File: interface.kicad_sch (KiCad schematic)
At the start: 6 parts, among them J2 M20-7810245, J3 M20-7812045, J4 M20-7812045

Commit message: Board is fully routed
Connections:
- net 12V: no longer names the net of J4.1 (+12V)
- net 12V: no longer J3.1 (+12V)
- no-connect marks 58 -> 60
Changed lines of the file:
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@@
   (junction (at 134.62 72.39) (diameter 0) (color 0 0 0 0)
-  )
-  (junction (at 73.66 46.99) (diameter 0) (color 0 0 0 0)
   )
   (junction (at 134.62 85.09) (diameter 0) (color 0 0 0 0)
@@
   (no_connect (at 77.47 92.71))
   (no_connect (at 102.87 92.71))
+  (no_connect (at 77.47 46.99))
   (no_connect (at 137.16 67.31))
   (no_connect (at 137.16 95.25))
@@
   (no_connect (at 102.87 77.47))
   (no_connect (at 137.16 62.23))
+  (no_connect (at 137.16 46.99))
   (no_connect (at 137.16 80.01))
   (no_connect (at 77.47 49.53))
@@
     (stroke (width 0) (type default))
   )
-  (wire (pts (xy 64.77 46.99) (xy 73.66 46.99))
-    (stroke (width 0) (type default))
-  )
   (wire (pts (xy 256.54 44.45) (xy 254 44.45))
     (stroke (width 0) (type default))
@@
     (stroke (width 0) (type default))
   )
-  (wire (pts (xy 133.35 43.18) (xy 133.35 46.99))
-    (stroke (width 0) (type default))
-  )
   (wire (pts (xy 238.76 91.44) (xy 238.76 93.98))
     (stroke (width 0) (type default))
@@
     (stroke (width 0) (type default))
   )
-  (wire (pts (xy 73.66 46.99) (xy 77.47 46.99))
-    (stroke (width 0) (type default))
-  )
   (wire (pts (xy 63.5 69.85) (xy 77.47 69.85))
     (stroke (width 0) (type default))
@@
     (stroke (width 0) (type default))
   )
-  (wire (pts (xy 73.66 43.18) (xy 73.66 46.99))
-    (stroke (width 0) (type default))
-  )
   (wire (pts (xy 105.41 85.09) (xy 105.41 104.14))
     (stroke (width 0) (type default))
@@
   )
   (wire (pts (xy 77.47 59.69) (xy 74.93 59.69))
-    (stroke (width 0) (type default))
-  )
-  (wire (pts (xy 133.35 46.99) (xy 137.16 46.99))
-    (stroke (width 0) (type default))
-  )
-  (wire (pts (xy 64.77 43.18) (xy 64.77 46.99))
     (stroke (width 0) (type default))
   )
@@
         (path "/b3f993c3-1966-49ed-ad69-98ff713d15d5/022f9d20-4e59-4748-8eac-9224ddae6c41"
           (reference "#PWR06") (unit 1)
-        )
-      )
-    )
-  )
-  (symbol (lib_id "sesa_power:12V") (at 133.35 43.18 0) (unit 1)
-    (in_bom yes) (on_board yes) (dnp no)
-    (property "Reference" "#PWR01" (at 133.35 40.64 0)
-      (effects (font (size 1.016 1.016)) hide)
-    )
-    (property "Value" "12V" (at 133.35 40.513 0)
-      (effects (font (size 1.27 1.27)))
-    )
-    (property "Footprint" "" (at 133.35 43.18 0)
-      (effects (font (size 1.27 1.27)))
-    )
-    (property "Datasheet" "" (at 133.35 43.18 0)
-      (effects (font (size 1.27 1.27)))
-    )
-    (pin "1")
-    (instances
-      (project "DMM_Module"
-        (path "/b3f993c3-1966-49ed-ad69-98ff713d15d5/022f9d20-4e59-4748-8eac-9224ddae6c41"
-          (reference "#PWR01") (unit 1)
         )
       )
@@
         )
       )
-    )
-  )
-  (symbol (lib_id "sesa_power:12V") (at 73.66 43.18 0) (unit 1)
-    (in_bom yes) (on_board yes) (dnp no)
-    (property "Reference" "#PWR04" (at 73.66 40.64 0)
-      (effects (font (size 1.016 1.016)) hide)
-    )
-    (property "Value" "12V" (at 73.66 40.513 0)
-      (effects (font (size 1.27 1.27)))
-    )
-    (property "Footprint" "" (at 73.66 43.18 0)
-      (effects (font (size 1.27 1.27)))
-    )
-    (property "Datasheet" "" (at 73.66 43.18 0)
-      (effects (font (size 1.27 1.27)))
-    )
-    (pin "1")
-    (instances
-      (project "DMM_Module"
-        (path "/b3f993c3-1966-49ed-ad69-98ff713d15d5/022f9d20-4e59-4748-8eac-9224ddae6c41"
-          (reference "#PWR04") (unit 1)
-        )
-      )
-    )
-  )
-  (symbol (lib_id "sesa_power:PWR_PORT") (at 64.77 43.18 0) (unit 1)
-    (in_bom yes) (on_board yes) (dnp no)
-    (property "Reference" "#PWR09" (at 64.77 40.64 0)
-      (effects (font (size 1.016 1.016)) hide)
-    )
-    (property "Value" "PWR_PORT" (at 64.77 40.513 0)
-      (effects (font (size 1.27 1.27)))
-    )
-    (property "Footprint" "" (at 64.77 43.18 0)
-      (effects (font (size 1.27 1.27)))
-    )
-    (property "Datasheet" "" (at 64.77 43.18 0)
-      (effects (font (size 1.27 1.27)))
-    )
-    (pin "1")
-    (instances
-      (project "DMM_Module"
-        (path "/b3f993c3-1966-49ed-ad69-98ff713d15d5/0095a40f-579d-4b0e-95e8-5fdd46ee20e8"
-          (reference "#PWR09") (unit 1)
-        )
-        (path "/b3f993c3-1966-49ed-ad69-98ff713d15d5/022f9d20-4e59-4748-8eac-9224ddae6c41"
-          (reference "#PWR060") (unit 1)
-        )
-      )

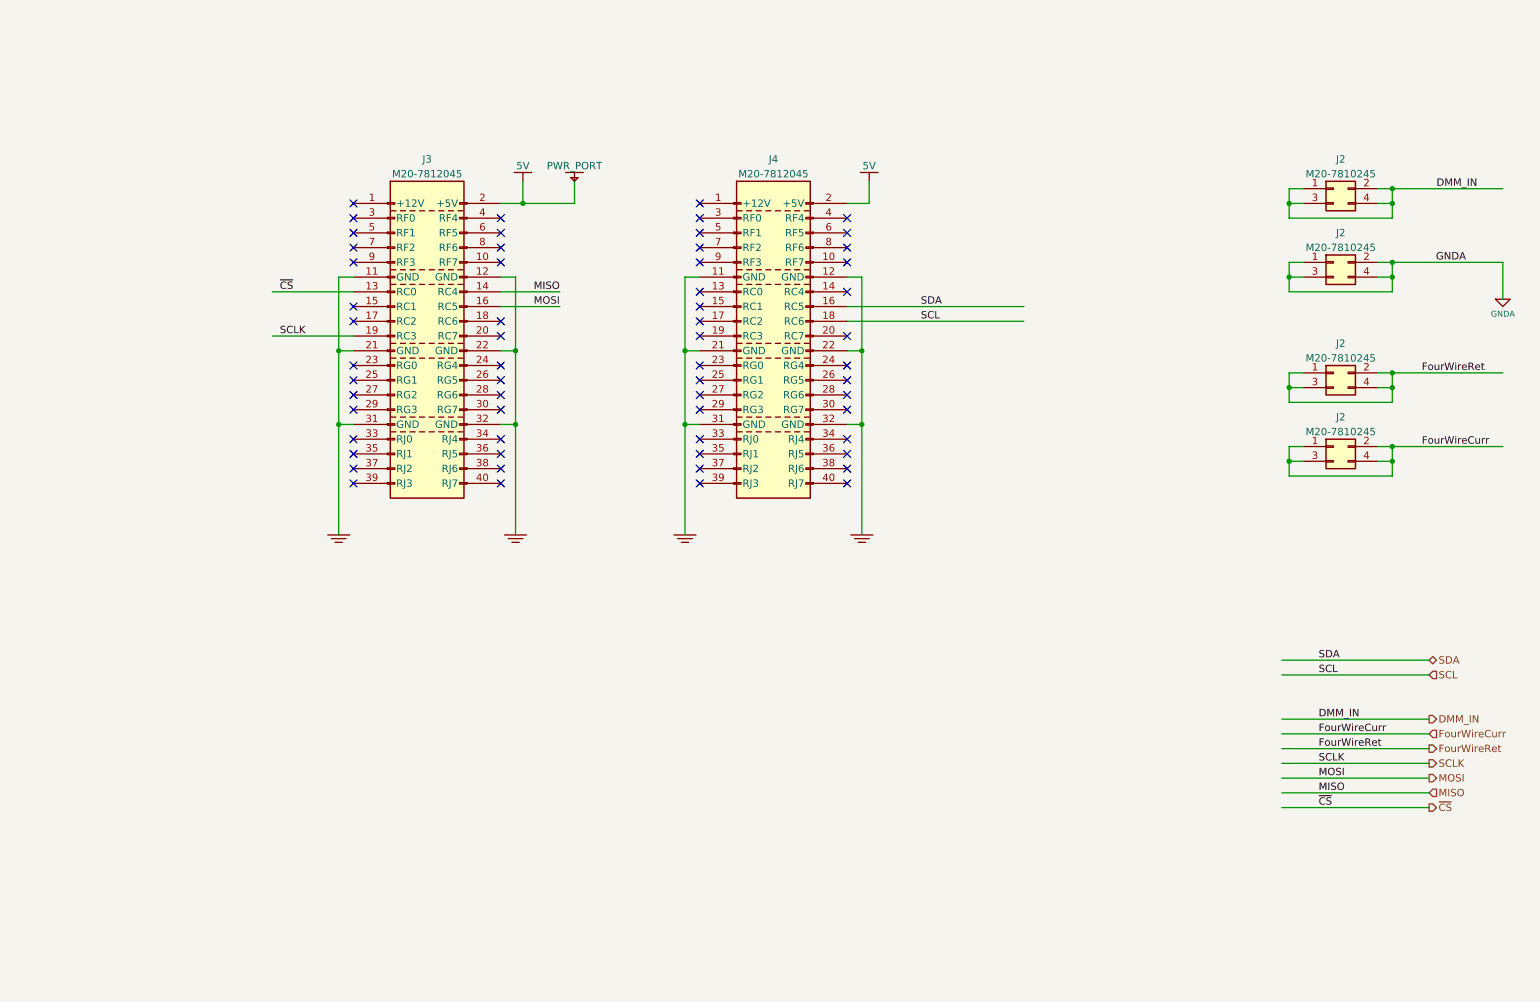
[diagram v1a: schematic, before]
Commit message: Added galvanic isolation
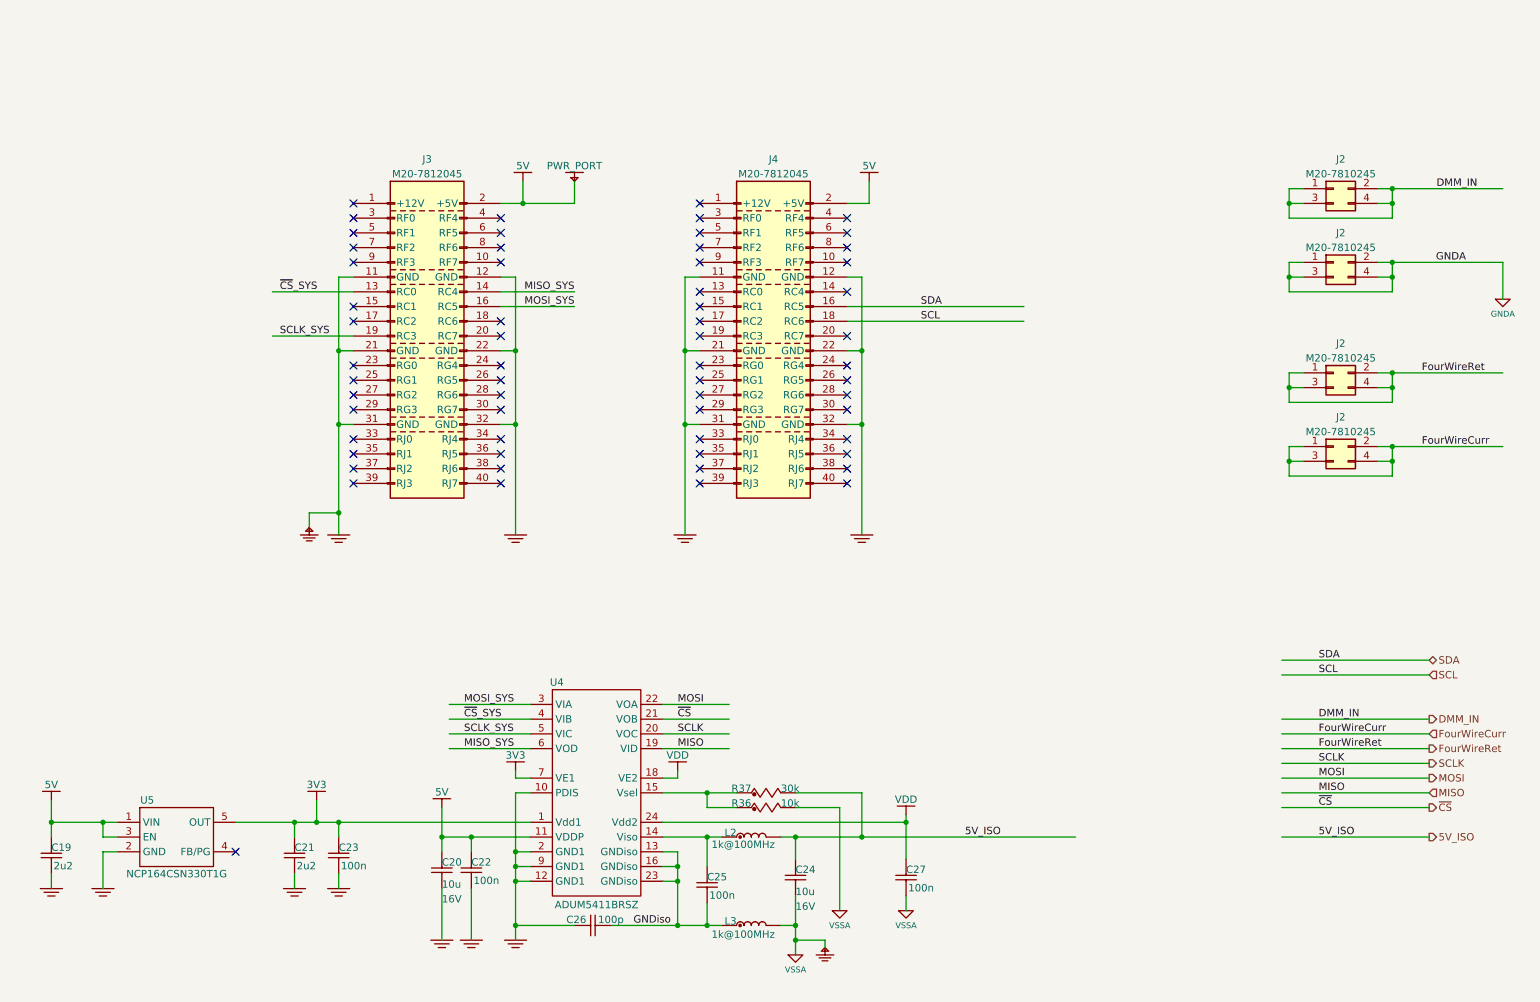
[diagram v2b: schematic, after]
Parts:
- added C19, C21: 2u2, Capacitor_SMD:C_0603_1608Metric, symbol cap_0603:2u2
- added C20, C24: 10u, Capacitor_SMD:C_0603_1608Metric, symbol cap_0603:10u_16v
- added C22, C23, C25, C27: 100n, Capacitor_SMD:C_0603_1608Metric, symbol cap_0603:100n
- added C26: 100p, Capacitor_SMD:C_0603_1608Metric, symbol cap_0603:100p
- added L2, L3: 1k@100MHz, Inductor_SMD:L_0603_1608Metric, symbol sesa_coil:fb_1k_0603
- added R36: 10k, Resistor_SMD:R_0603_1608Metric, symbol res_0603:10k
- added R37: 30k, Resistor_SMD:R_0603_1608Metric, symbol res_0603:30k
- added U4: ADUM5411BRSZ, Package_SO:SSOP-24_5.3x8.2mm_P0.65mm, symbol sesa_ic_interface:ADUM5411
- added U5: NCP164CSN330T1G, Package_TO_SOT_SMD:SOT-23-5, symbol sesa_ic_power:NCP164CSN330T1G
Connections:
- net 5V: now also C19.2, C20.2, C22.2, U4.11 (VDDP), U5.1 (VIN), U5.3 (EN)
- net GND: now also C19.1, C20.1, C21.1, C22.1, C23.1, C26.2, U4.10 (PDIS), U4.12 (GND1), U4.2 (GND1), U4.9 (GND1), U5.2 (GND)
- net MISO: now also U4.19 (VID); no longer J3.14 (RC4)
- net MOSI: now also U4.22 (VOA); no longer J3.16 (RC5)
- net SCLK: now also U4.20 (VOC); no longer J3.19 (RC3)
- net ~{CS}: now also U4.21 (VOB); no longer J3.13 (RC0)
- new net: R36.1, R37.1, U4.15 (Vsel)
- new net: C25.2, L2.1, U4.14 (Viso)
- new net 3V3: C21.2, C23.2, U4.1 (Vdd1), U4.7 (VE1), U5.5 (OUT)
- new net 5V_ISO: C24.2, L2.2, R37.2
- new net GNDiso: C25.1, C26.1, L3.1, U4.13 (GNDiso), U4.16 (GNDiso), U4.23 (GNDiso)
- new net MISO_SYS: J3.14 (RC4), U4.6 (VOD)
- new net MOSI_SYS: J3.16 (RC5), U4.3 (VIA)
- new net SCLK_SYS: J3.19 (RC3), U4.5 (VIC)
- new net VDD: C27.2, U4.18 (VE2), U4.24 (Vdd2)
- new net VSSA: C24.1, C27.1, L3.2, R36.2
- new net ~{CS}_SYS: J3.13 (RC0), U4.4 (VIB)
- no-connect marks 60 -> 61

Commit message: Schematics updated with current protection and EEPROM
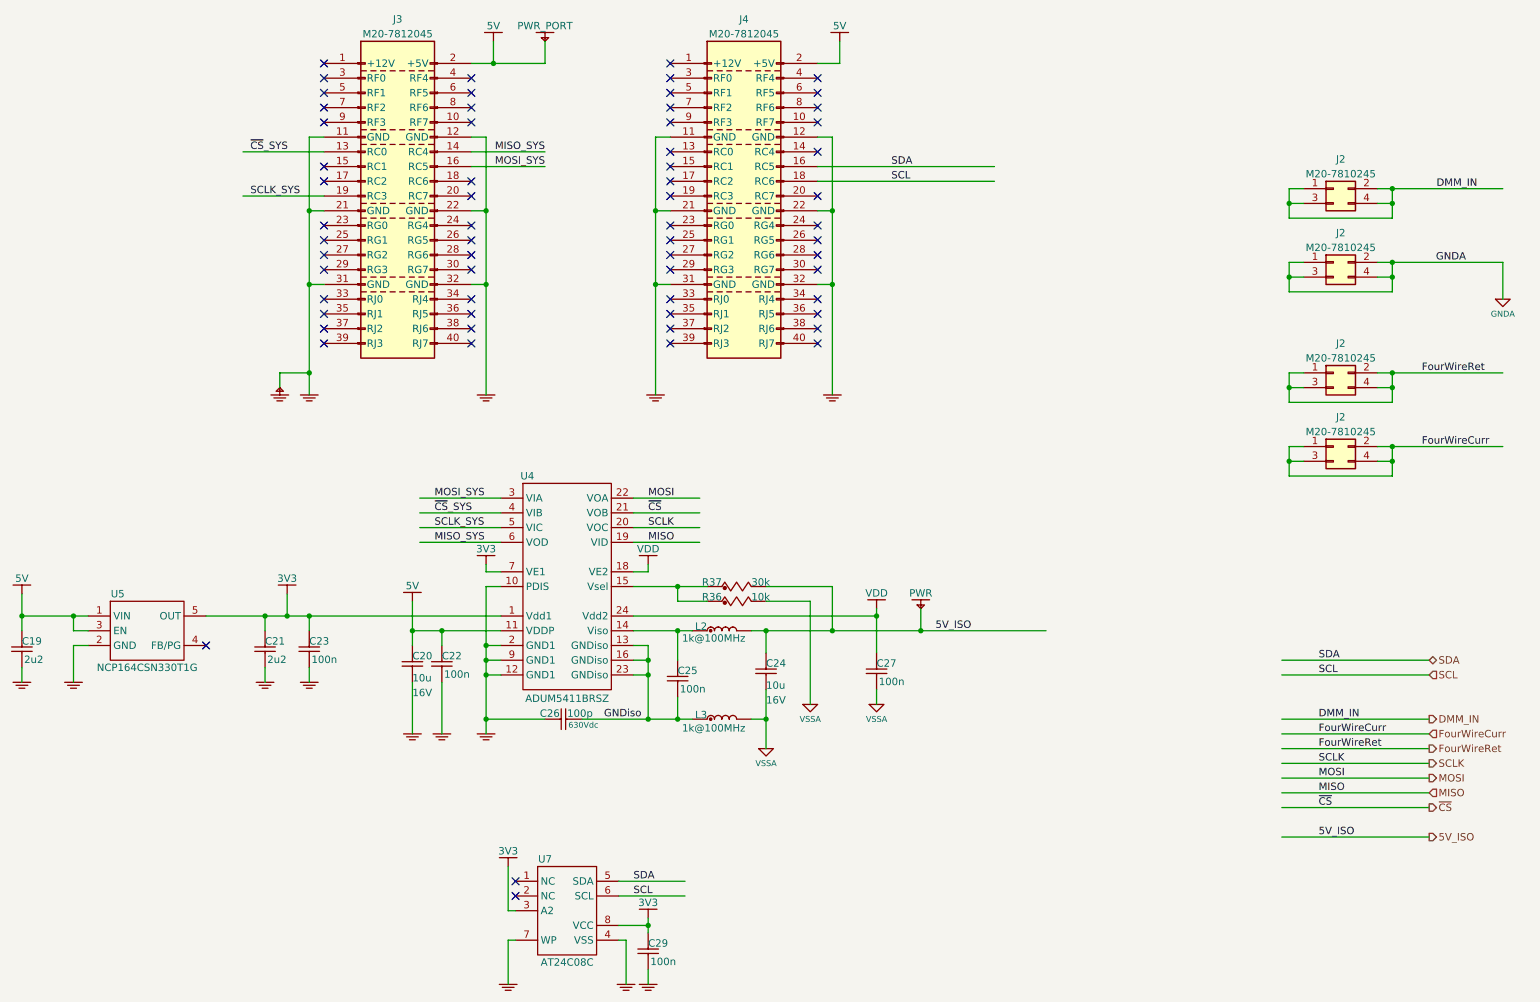
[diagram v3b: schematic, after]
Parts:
- removed C26: 100p, Capacitor_SMD:C_0603_1608Metric, symbol cap_0603:100p
- added C26: 100p, Capacitor_SMD:C_1206_3216Metric, symbol cap_1206:100p_HV
- added C29: 100n, Capacitor_SMD:C_0603_1608Metric, symbol cap_0603:100n
- added U7: AT24C08C, Package_SO:TSSOP-8_4.4x3mm_P0.65mm, symbol sesa_ic_memory:AT24C08C-XHM-T
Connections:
- net 3V3: now also C29.2, U7.3 (A2), U7.8 (VCC)
- net GND: now also C26.2, C29.1, U7.4 (VSS), U7.7 (WP)
- net GNDiso: now also C26.1
- net SCL: now also U7.6 (SCL)
- net SDA: now also U7.5 (SDA)
- no-connect marks 61 -> 63
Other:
- moved on the sheet: C19, C20, C21, C22, C23, C24, C25, C27, J3, J4, L2, L3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
